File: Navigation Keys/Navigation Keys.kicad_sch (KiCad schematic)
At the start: 20 parts

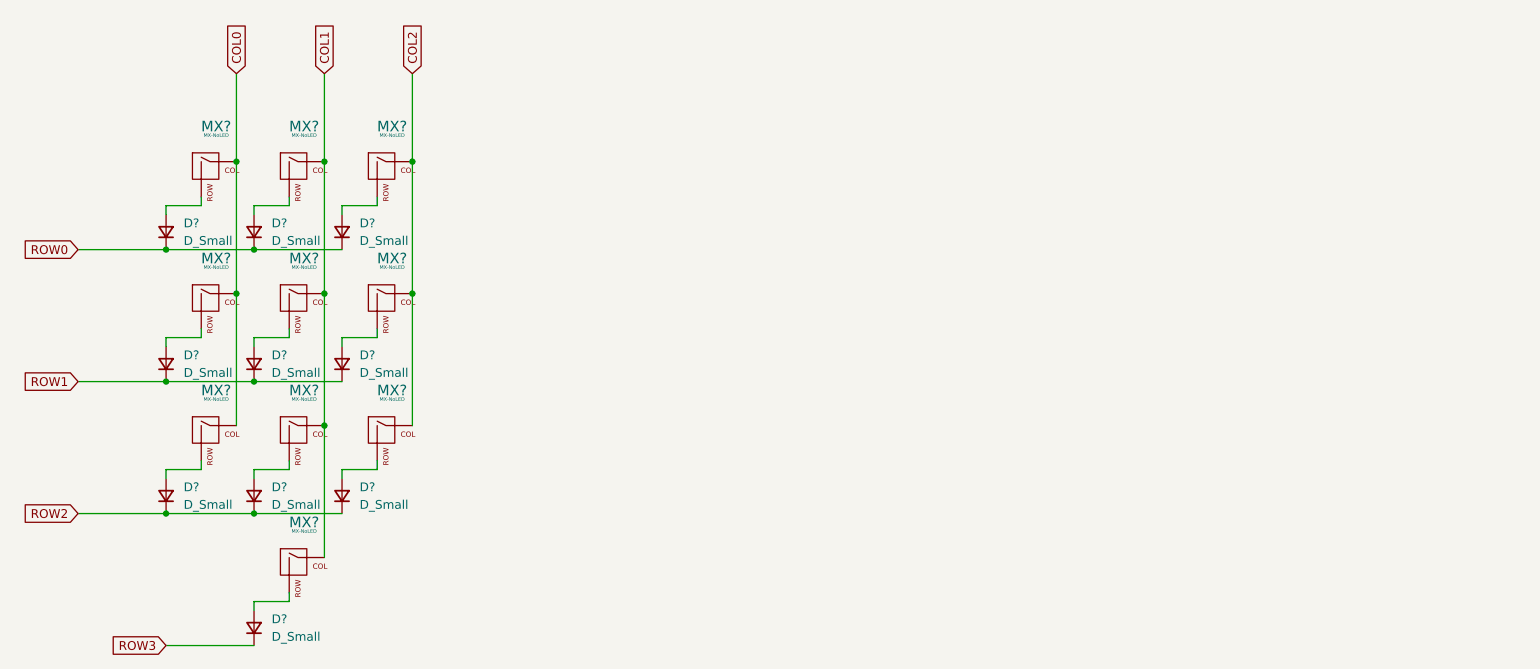
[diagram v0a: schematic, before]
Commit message: Added connectors, labeled keys
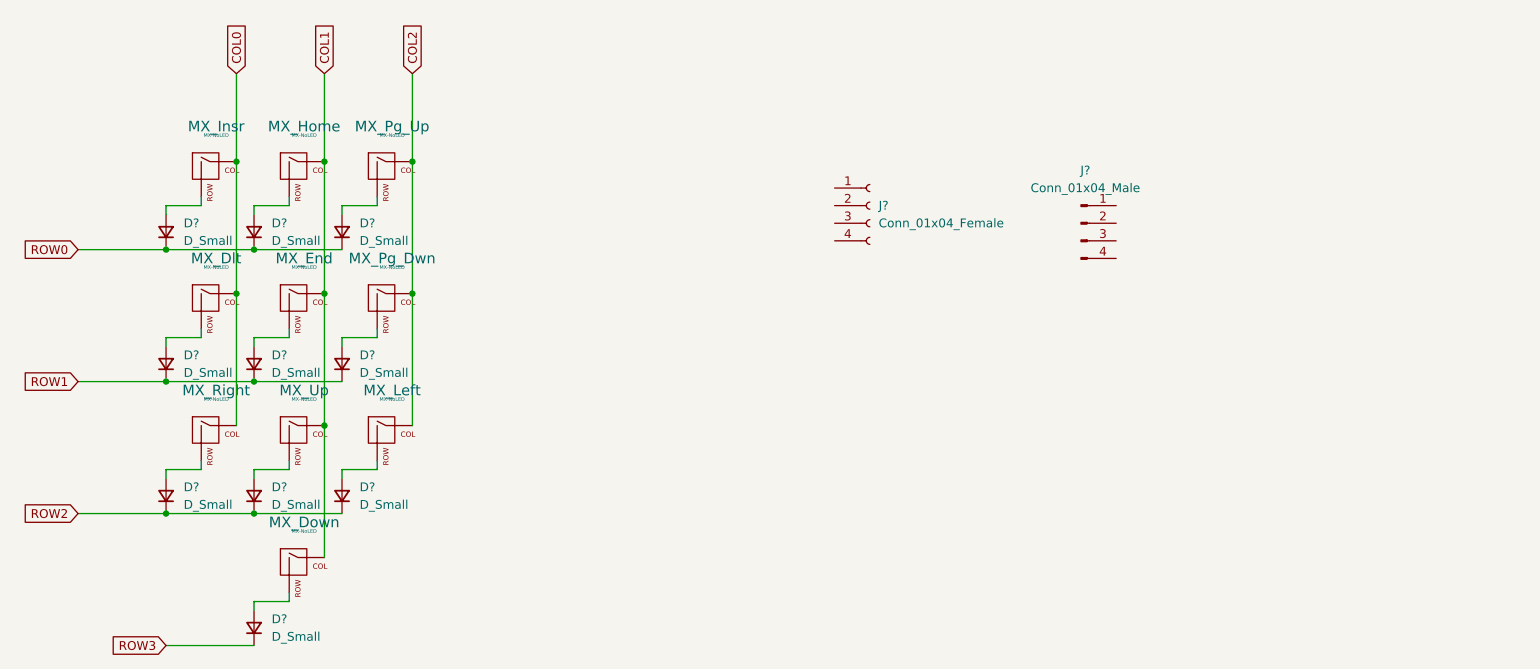
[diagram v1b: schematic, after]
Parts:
- added J?: Conn_01x04_Male, symbol Connector:Conn_01x04_Male
- added J?: Conn_01x04_Female, symbol Connector:Conn_01x04_Female
- gave numbers to parts that had none: 10
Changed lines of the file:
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@@
     )
+  )
+  (symbol (lib_id "Connector:Conn_01x04_Male") (at 187.96 49.53 0) (unit 1)
+    (in_bom yes) (on_board yes) (fields_autoplaced)
+    (property "Reference" "J?" (id 0) (at 188.595 41.91 0))
+    (property "Value" "Conn_01x04_Male" (id 1) (at 188.595 44.45 0))
+    (property "Footprint" "" (id 2) (at 187.96 49.53 0)
+      (effects (font (size 1.27 1.27)) hide)
+    )
+    (property "Datasheet" "~" (id 3) (at 187.96 49.53 0)
+      (effects (font (size 1.27 1.27)) hide)
+    )
+    (pin "1")
+    (pin "2")
+    (pin "3")
+    (pin "4")
   )
   (symbol (lib_id "Device:D_Small") (at 81.28 69.85 90) (unit 1)
@@
     (pin "2")
   )
+  (symbol (lib_id "Connector:Conn_01x04_Female") (at 157.48 46.99 0) (unit 1)
+    (in_bom yes) (on_board yes) (fields_autoplaced)
+    (property "Reference" "J?" (id 0) (at 158.75 46.9899 0)
+      (effects (font (size 1.27 1.27)) (justify left))
+    )
+    (property "Value" "Conn_01x04_Female" (id 1) (at 158.75 49.5299 0)
+      (effects (font (size 1.27 1.27)) (justify left))
+    )
+    (property "Footprint" "" (id 2) (at 157.48 46.99 0)
+      (effects (font (size 1.27 1.27)) hide)
+    )
+    (property "Datasheet" "~" (id 3) (at 157.48 46.99 0)
+      (effects (font (size 1.27 1.27)) hide)
+    )
+    (pin "1")
+    (pin "2")
+    (pin "3")
+    (pin "4")
+  )
   (symbol (lib_id "Device:D_Small") (at 55.88 88.9 90) (unit 1)
     (in_bom yes) (on_board yes) (fields_autoplaced)
@@
   (symbol (lib_id "MX_Alps_Hybrid:MX-NoLED") (at 62.23 80.01 0) (unit 1)
     (in_bom yes) (on_board yes) (fields_autoplaced)
-    (property "Reference" "MX?" (id 0) (at 63.1156 73.66 0)
+    (property "Reference" "MX_Right" (id 0) (at 63.1156 73.66 0)
       (effects (font (size 1.524 1.524)))
     )
@@
   (symbol (lib_id "MX_Alps_Hybrid:MX-NoLED") (at 87.63 60.96 0) (unit 1)
     (in_bom yes) (on_board yes) (fields_autoplaced)
-    (property "Reference" "MX?" (id 0) (at 88.5156 54.61 0)
+    (property "Reference" "MX_Pg_Dwn" (id 0) (at 88.5156 54.61 0)
       (effects (font (size 1.524 1.524)))
     )
@@
   (symbol (lib_id "MX_Alps_Hybrid:MX-NoLED") (at 74.93 99.06 0) (unit 1)
     (in_bom yes) (on_board yes) (fields_autoplaced)
-    (property "Reference" "MX?" (id 0) (at 75.8156 92.71 0)
+    (property "Reference" "MX_Down" (id 0) (at 75.8156 92.71 0)
       (effects (font (size 1.524 1.524)))
     )
@@
   (symbol (lib_id "MX_Alps_Hybrid:MX-NoLED") (at 87.63 80.01 0) (unit 1)
     (in_bom yes) (on_board yes) (fields_autoplaced)
-    (property "Reference" "MX?" (id 0) (at 88.5156 73.66 0)
+    (property "Reference" "MX_Left" (id 0) (at 88.5156 73.66 0)
       (effects (font (size 1.524 1.524)))
     )
@@
   (symbol (lib_id "MX_Alps_Hybrid:MX-NoLED") (at 74.93 41.91 0) (unit 1)
     (in_bom yes) (on_board yes) (fields_autoplaced)
-    (property "Reference" "MX?" (id 0) (at 75.8156 35.56 0)
+    (property "Reference" "MX_Home" (id 0) (at 75.8156 35.56 0)
       (effects (font (size 1.524 1.524)))
     )
@@
   (symbol (lib_id "MX_Alps_Hybrid:MX-NoLED") (at 74.93 80.01 0) (unit 1)
     (in_bom yes) (on_board yes) (fields_autoplaced)
-    (property "Reference" "MX?" (id 0) (at 75.8156 73.66 0)
+    (property "Reference" "MX_Up" (id 0) (at 75.8156 73.66 0)
       (effects (font (size 1.524 1.524)))
     )
@@
   (symbol (lib_id "MX_Alps_Hybrid:MX-NoLED") (at 74.93 60.96 0) (unit 1)
     (in_bom yes) (on_board yes) (fields_autoplaced)
-    (property "Reference" "MX?" (id 0) (at 75.8156 54.61 0)
+    (property "Reference" "MX_End" (id 0) (at 75.8156 54.61 0)
       (effects (font (size 1.524 1.524)))
     )
@@
   (symbol (lib_id "MX_Alps_Hybrid:MX-NoLED") (at 62.23 41.91 0) (unit 1)
     (in_bom yes) (on_board yes) (fields_autoplaced)
-    (property "Reference" "MX?" (id 0) (at 63.1156 35.56 0)
+    (property "Reference" "MX_Insr" (id 0) (at 63.1156 35.56 0)
       (effects (font (size 1.524 1.524)))
     )
@@
   (symbol (lib_id "MX_Alps_Hybrid:MX-NoLED") (at 62.23 60.96 0) (unit 1)
     (in_bom yes) (on_board yes) (fields_autoplaced)
-    (property "Reference" "MX?" (id 0) (at 63.1156 54.61 0)
+    (property "Reference" "MX_Dlt" (id 0) (at 63.1156 54.61 0)
       (effects (font (size 1.524 1.524)))
     )
@@
   (symbol (lib_id "MX_Alps_Hybrid:MX-NoLED") (at 87.63 41.91 0) (unit 1)
     (in_bom yes) (on_board yes) (fields_autoplaced)
-    (property "Reference" "MX?" (id 0) (at 88.5156 35.56 0)
+    (property "Reference" "MX_Pg_Up" (id 0) (at 88.5156 35.56 0)
       (effects (font (size 1.524 1.524)))
     )
@@
       (reference "D?") (unit 1) (value "D_Small") (footprint "")
     )
+    (path "/07422982-bf5c-4780-9ce4-978e8ad9e4c3"
+      (reference "J?") (unit 1) (value "Conn_01x04_Male") (footprint "")
+    )
+    (path "/2bc40c82-8234-4f78-ac50-132af808e760"
+      (reference "J?") (unit 1) (value "Conn_01x04_Female") (footprint "")
+    )
+    (path "/d83f6aba-3d42-4ab8-9bba-b080aea0423e"
+      (reference "MX_Dlt") (unit 1) (value "MX-NoLED") (footprint "")
+    )
+    (path "/934fa8ee-8ae0-42e8-9350-699da123a2c4"
+      (reference "MX_Down") (unit 1) (value "MX-NoLED") (footprint "")
+    )
+    (path "/c5fcca55-9949-477e-aaa3-d95c92b92f27"
+      (reference "MX_End") (unit 1) (value "MX-NoLED") (footprint "")
+    )
+    (path "/9a16343e-6f61-4ebe-b51c-dff101147388"
+      (reference "MX_Home") (unit 1) (value "MX-NoLED") (footprint "")
+    )
+    (path "/d6afd8f2-b5b9-4c47-a0a3-bf1c598b797d"
+      (reference "MX_Insr") (unit 1) (value "MX-NoLED") (footprint "")
+    )
+    (path "/98e20c87-b945-4996-a29a-4ed0966889ee"
+      (reference "MX_Left") (unit 1) (value "MX-NoLED") (footprint "")
+    )
+    (path "/92060247-a0b1-42b7-904e-a7d6b0ae5b55"
+      (reference "MX_Pg_Dwn") (unit 1) (value "MX-NoLED") (footprint "")
+    )
+    (path "/d85858a2-ba0c-409f-af03-29d5c520f5a1"
+      (reference "MX_Pg_Up") (unit 1) (value "MX-NoLED") (footprint "")
+    )
     (path "/40f879de-b344-4453-a74f-61b1e4bc3990"
-      (reference "MX?") (unit 1) (value "MX-NoLED") (footprint "")
-    )
-    (path "/92060247-a0b1-42b7-904e-a7d6b0ae5b55"
-      (reference "MX?") (unit 1) (value "MX-NoLED") (footprint "")
-    )
-    (path "/934fa8ee-8ae0-42e8-9350-699da123a2c4"
-      (reference "MX?") (unit 1) (value "MX-NoLED") (footprint "")
-    )
-    (path "/98e20c87-b945-4996-a29a-4ed0966889ee"
-      (reference "MX?") (unit 1) (value "MX-NoLED") (footprint "")
-    )
-    (path "/9a16343e-6f61-4ebe-b51c-dff101147388"
-      (reference "MX?") (unit 1) (value "MX-NoLED") (footprint "")
+      (reference "MX_Right") (unit 1) (value "MX-NoLED") (footprint "")
     )
     (path "/a02abd0a-f87e-41f6-88a7-83569702db44"
-      (reference "MX?") (unit 1) (value "MX-NoLED") (footprint "")
-    )
-    (path "/c5fcca55-9949-477e-aaa3-d95c92b92f27"
-      (reference "MX?") (unit 1) (value "MX-NoLED") (footprint "")
-    )
-    (path "/d6afd8f2-b5b9-4c47-a0a3-bf1c598b797d"
-      (reference "MX?") (unit 1) (value "MX-NoLED") (footprint "")
-    )
-    (path "/d83f6aba-3d42-4ab8-9bba-b080aea0423e"
-      (reference "MX?") (unit 1) (value "MX-NoLED") (footprint "")
-    )
-    (path "/d85858a2-ba0c-409f-af03-29d5c520f5a1"
-      (reference "MX?") (unit 1) (value "MX-NoLED") (footprint "")
-    )
-  )
+      (reference "MX_Up") (unit 1) (value "MX-NoLED") (footprint "")
+    )
+  )

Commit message: Added connectors, labeled schematic
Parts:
- removed J?: Conn_01x04_Male, symbol Connector:Conn_01x04_Male
- removed J?: Conn_01x04_Female, symbol Connector:Conn_01x04_Female
- added J1: Conn_01x05_Female, symbol Connector:Conn_01x05_Female
- added J2: Conn_01x05_Male, symbol Connector:Conn_01x05_Male
- added R1, R2: R_Small, symbol Device:R_Small
- gave numbers to parts that had none: 10
- renumbered MX_Dlt to MX_Dlt1, MX_Down to MX_Down1, MX_End to MX_End1, MX_Home to MX_Home1, MX_Insr to MX_Insr1, MX_Left to MX_Left1, MX_Pg_Dwn to MX_Pg_Dwn1, MX_Pg_Up to MX_Pg_Up1, MX_Right to MX_Right1, MX_Up to MX_Up1
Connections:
- new net: J2.3 (Pin_3), R2.1
- new net: J1.3 (Pin_3), R1.2
- new net GND: J1.5 (Pin_5), J2.5 (Pin_5)
- new net IN: R2.2
- new net OUT: R1.1
- new net VCC: J1.1 (Pin_1), J2.1 (Pin_1)

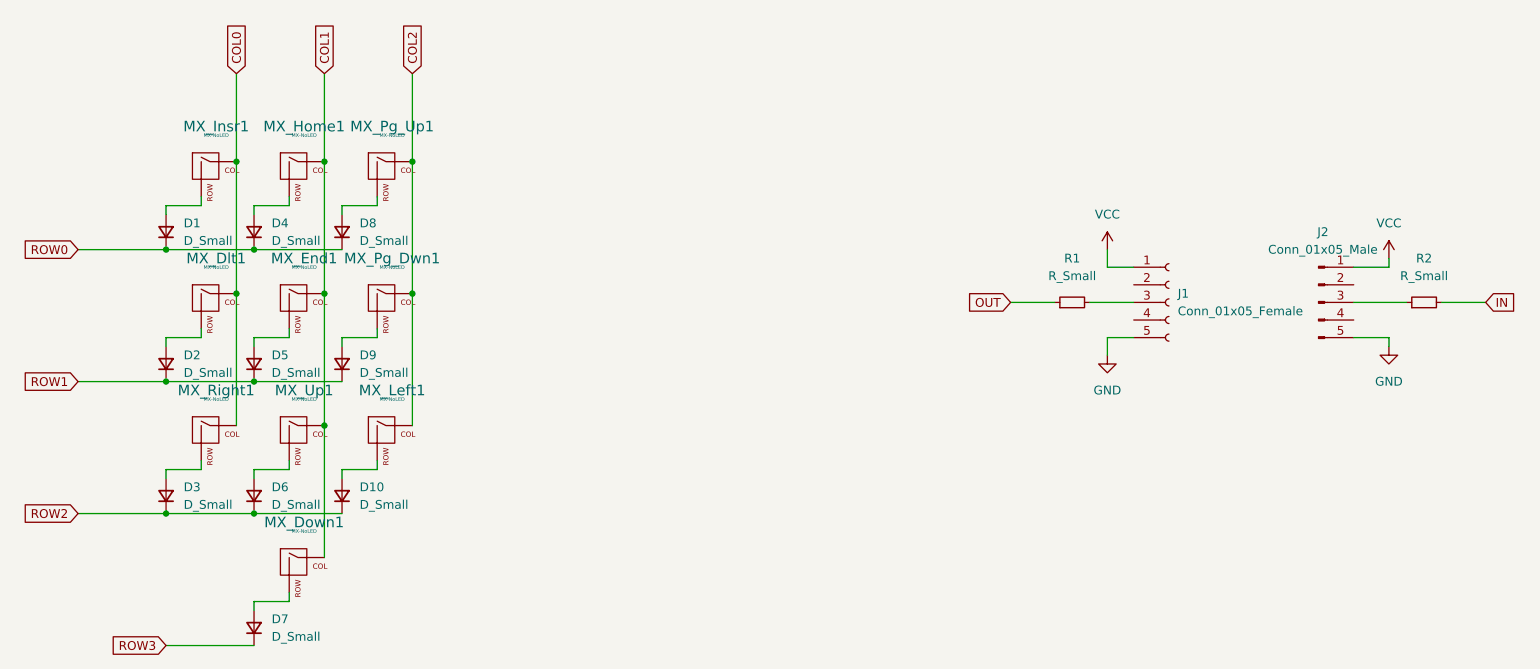
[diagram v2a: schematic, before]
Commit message: Assigned footprints
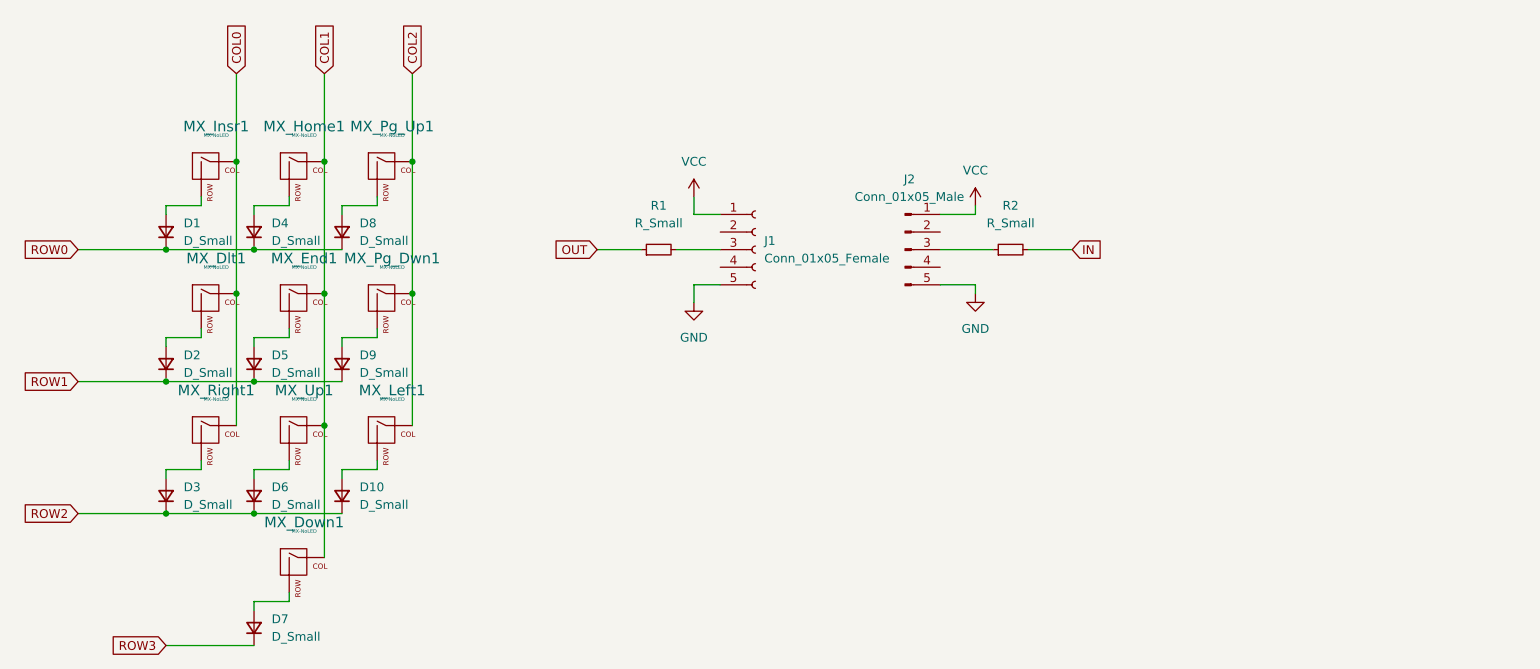
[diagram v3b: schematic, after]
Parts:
- D1, D10, D2, D3, D4, D5, D6, D7, D8, D9: footprint (none) -> Diode_SMD:D_SOD-123
- J1, J2: footprint (none) -> Connector_JST:JST_PH_S5B-PH-K_1x05_P2.00mm_Horizontal
- MX_Dlt1, MX_Down1, MX_End1, MX_Home1, MX_Insr1, MX_Left1, MX_Pg_Dwn1, MX_Pg_Up1, MX_Right1, MX_Up1: footprint (none) -> MX_Alps_Hybrid:MX-1U-NoLED
- R1, R2: footprint (none) -> Resistor_SMD:R_0805_2012Metric
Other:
- moved on the sheet: J1, J2, R1, R2
